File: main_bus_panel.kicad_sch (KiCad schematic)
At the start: 33 parts

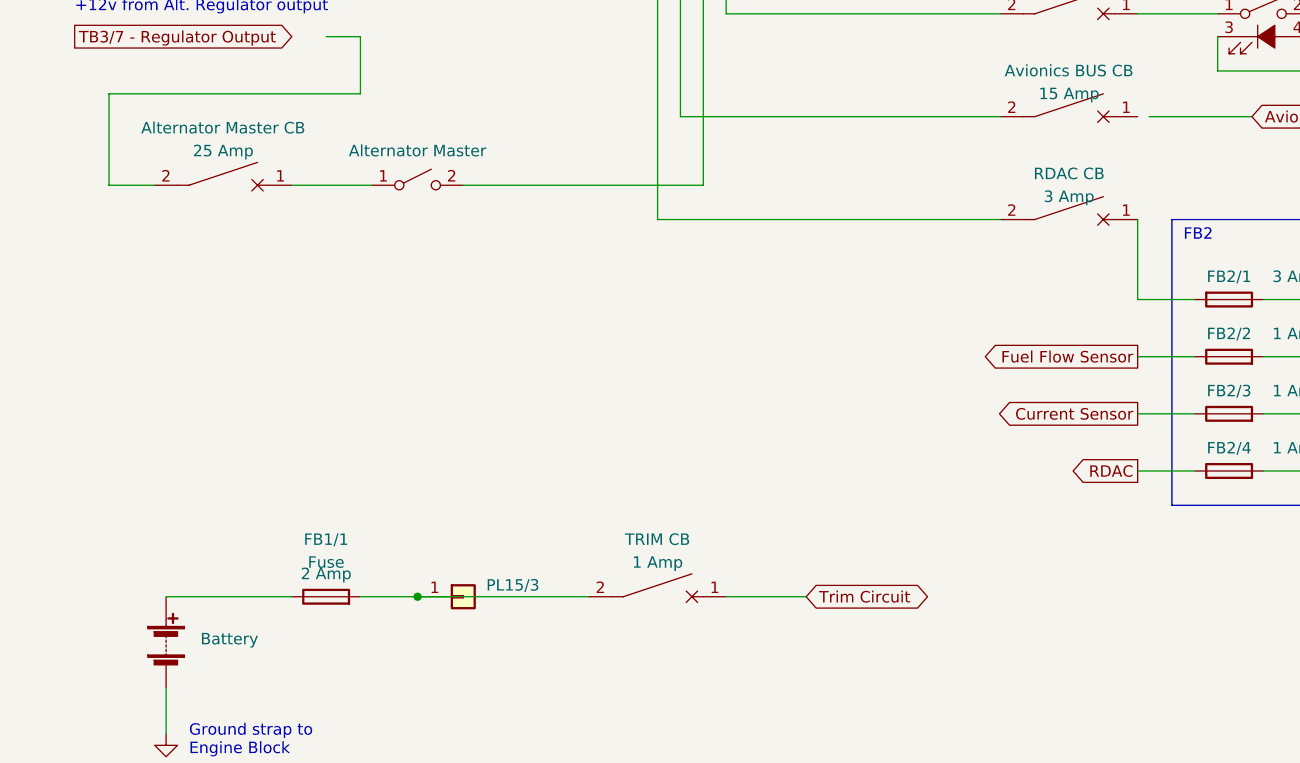
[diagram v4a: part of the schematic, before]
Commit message: Added Fuel Flow Sensor
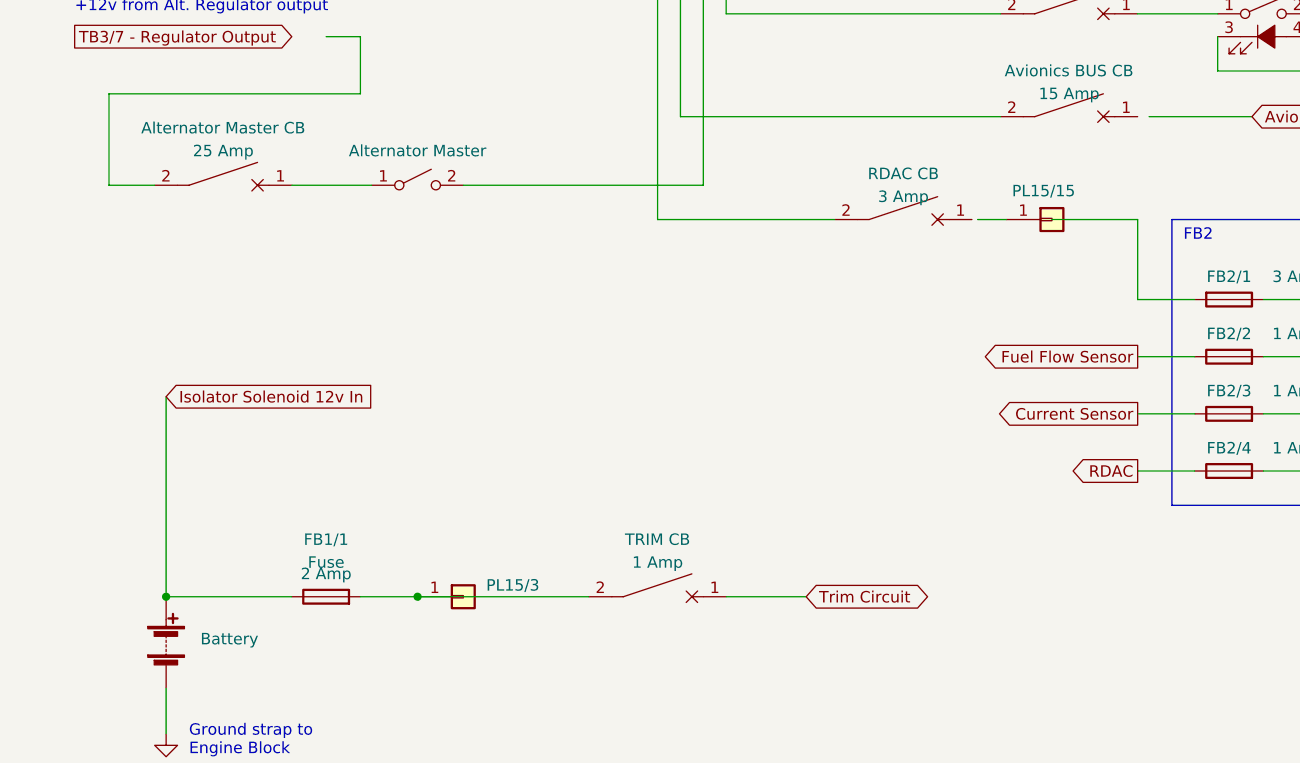
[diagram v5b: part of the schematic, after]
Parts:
- added PL15/15: Conn_01x01, symbol Connector_Generic:Conn_01x01
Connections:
- net Isolator Solenoid 12v In: now reaches BT?.1 (+), FB1/1.1
- net at FB2/1.2: no longer CB?.1
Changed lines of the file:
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@@
   (junction (at 101.6 57.15) (diameter 0) (color 0 0 0 0)
   )
+  (junction (at 29.21 167.64) (diameter 0) (color 0 0 0 0)
+  )
   (junction (at 109.22 46.99) (diameter 0) (color 0 0 0 0)
   )
@@
     (stroke (width 0) (type default) (color 0 0 0 0))
   )
+  (wire (pts (xy 29.21 167.64) (xy 43.18 167.64))
+    (stroke (width 0) (type default) (color 0 0 0 0))
+  )
   (wire (pts (xy 101.6 46.99) (xy 101.6 57.15))
     (stroke (width 0) (type default) (color 0 0 0 0))
@@
     (stroke (width 0) (type default) (color 0 0 0 0))
   )
+  (wire (pts (xy 137.16 125.73) (xy 137.16 134.62))
+    (stroke (width 0) (type default) (color 0 0 0 0))
+  )
   (wire (pts (xy 237.49 135.89) (xy 242.57 135.89))
     (stroke (width 0) (type default) (color 0 0 0 0))
@@
     (stroke (width 0) (type default) (color 0 0 0 0))
   )
-  (wire (pts (xy 137.16 125.73) (xy 137.16 134.62))
-    (stroke (width 0) (type default) (color 0 0 0 0))
-  )
   (wire (pts (xy 137.16 140.97) (xy 143.51 140.97))
     (stroke (width 0) (type default) (color 0 0 0 0))
@@
     (stroke (width 0) (type default) (color 0 0 0 0))
   )
+  (wire (pts (xy 119.38 125.73) (xy 122.555 125.73))
+    (stroke (width 0) (type default) (color 0 0 0 0))
+  )
   (wire (pts (xy 146.05 105.41) (xy 146.05 109.22))
     (stroke (width 0) (type default) (color 0 0 0 0))
@@
     (stroke (width 0) (type default) (color 0 0 0 0))
   )
-  (wire (pts (xy 167.64 102.87) (xy 175.26 102.87))
-    (stroke (width 0) (type default) (color 0 0 0 0))
-  )
   (wire (pts (xy 29.21 177.8) (xy 29.21 182.88))
+    (stroke (width 1) (type default) (color 0 0 0 0))
+  )
+  (wire (pts (xy 167.64 102.87) (xy 175.26 102.87))
     (stroke (width 0) (type default) (color 0 0 0 0))
   )
@@
     (stroke (width 0) (type default) (color 0 0 0 0))
   )
-  (wire (pts (xy 83.82 125.73) (xy 121.92 125.73))
+  (wire (pts (xy 83.82 125.73) (xy 103.505 125.73))
     (stroke (width 0) (type default) (color 0 0 0 0))
   )
@@
     (stroke (width 0) (type default) (color 0 0 0 0))
   )
-  (wire (pts (xy 29.21 167.64) (xy 43.18 167.64))
-    (stroke (width 0) (type default) (color 0 0 0 0))
-  )
   (wire (pts (xy 93.98 91.44) (xy 121.92 91.44))
     (stroke (width 0) (type default) (color 0 0 0 0))
@@
     (stroke (width 0) (type default) (color 0 0 0 0))
   )
+  (wire (pts (xy 127.635 125.73) (xy 137.16 125.73))
+    (stroke (width 0) (type default) (color 0 0 0 0))
+  )
+  (wire (pts (xy 29.21 145.415) (xy 29.21 167.64))
+    (stroke (width 1) (type default) (color 0 0 0 0))
+  )
   (wire (pts (xy 137.16 147.32) (xy 143.51 147.32))
     (stroke (width 0) (type default) (color 0 0 0 0))
@@
     )
   )
+  (global_label "Isolator Solenoid 12v In" (shape input) (at 29.21 145.415 0) (fields_autoplaced)
+    (effects (font (size 1.27 1.27)) (justify left))
+    (property "Intersheet References" "${INTERSHEET_REFS}" (id 0) (at 55.0879 145.3356 0)
+      (effects (font (size 1.27 1.27)) (justify left) hide)
+    )
+  )
   (global_label "RDAC" (shape output) (at 137.16 153.67 180) (fields_autoplaced)
     (effects (font (size 1.27 1.27)) (justify right))
@@
     (pin "2")
   )
-  (symbol (lib_id "Device:CircuitBreaker_1P") (at 129.54 125.73 270) (unit 1)
+  (symbol (lib_id "Device:CircuitBreaker_1P") (at 111.125 125.73 270) (unit 1)
     (in_bom yes) (on_board yes)
-    (property "Reference" "CB?" (id 0) (at 129.54 118.11 90)
+    (property "Reference" "CB?" (id 0) (at 111.125 118.11 90)
       (effects (font (size 1.27 1.27)) hide)
     )
-    (property "Value" "RDAC CB" (id 1) (at 129.54 120.65 90))
-    (property "Footprint" "" (id 2) (at 129.54 125.73 0)
+    (property "Value" "RDAC CB" (id 1) (at 111.125 120.65 90))
+    (property "Footprint" "" (id 2) (at 111.125 125.73 0)
       (effects (font (size 1.27 1.27)) hide)
     )
-    (property "Datasheet" "~" (id 3) (at 129.54 125.73 0)
+    (property "Datasheet" "~" (id 3) (at 111.125 125.73 0)
       (effects (font (size 1.27 1.27)) hide)
     )
-    (property "Rating" "3 Amp" (id 4) (at 129.54 123.19 90))
+    (property "Rating" "3 Amp" (id 4) (at 111.125 123.19 90))
     (pin "1")
     (pin "2")
@@
     (pin "3")
   )
+  (symbol (lib_id "Connector_Generic:Conn_01x01") (at 127.635 125.73 0) (unit 1)
+    (in_bom yes) (on_board yes)
+    (property "Reference" "PL15/15" (id 0) (at 123.19 122.555 0)
+      (effects (font (size 1.27 1.27)) (justify left))
+    )
+    (property "Value" "Conn_01x01" (id 1) (at 130.81 126.9999 0)
+      (effects (font (size 1.27 1.27)) (justify left) hide)
+    )
+    (property "Footprint" "" (id 2) (at 127.635 125.73 0)
+      (effects (font (size 1.27 1.27)) hide)
+    )
+    (property "Datasheet" "~" (id 3) (at 127.635 125.73 0)
+      (effects (font (size 1.27 1.27)) hide)
+    )
+    (pin "1")
+  )
   (symbol (lib_id "Switch:SW_SPST") (at 74.93 21.59 0) (unit 1)
